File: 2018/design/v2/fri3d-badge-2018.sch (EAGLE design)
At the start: 136 parts

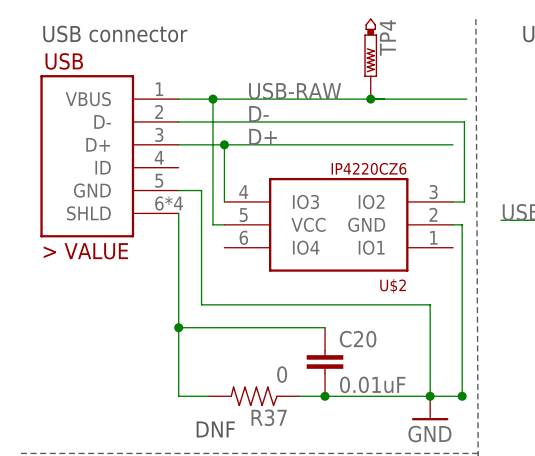
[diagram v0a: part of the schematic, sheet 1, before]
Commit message: fixed incorrect footprint for sx1308
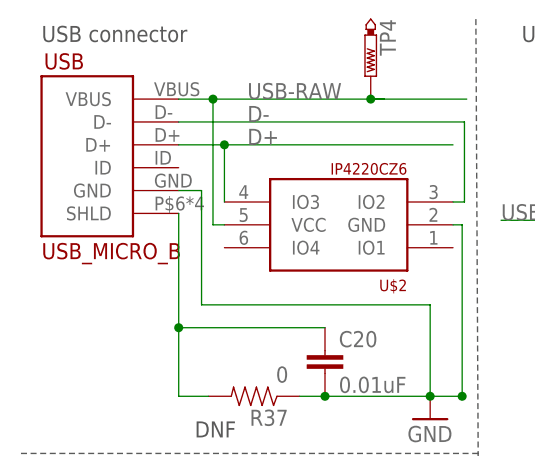
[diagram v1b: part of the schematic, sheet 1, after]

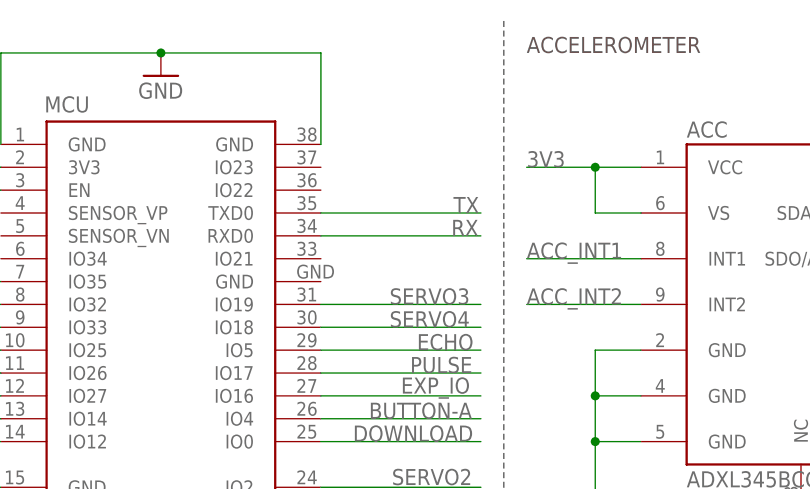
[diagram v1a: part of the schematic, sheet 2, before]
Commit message: added 3 missing traces/connections to ESP
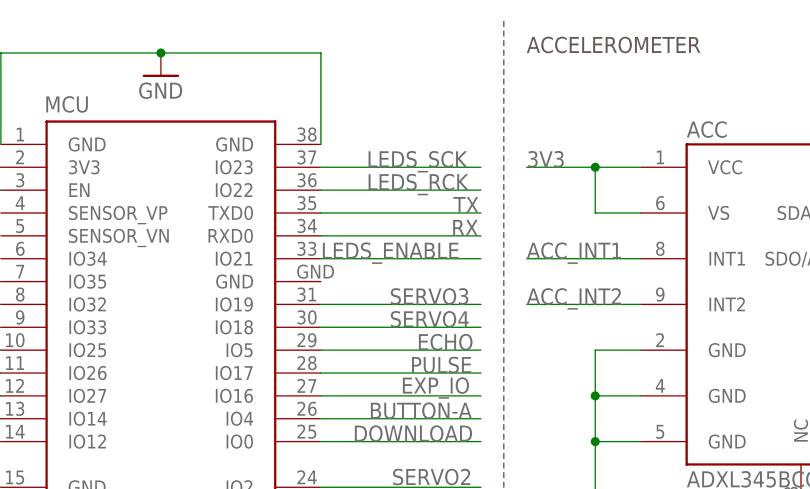
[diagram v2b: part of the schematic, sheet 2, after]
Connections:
- net LEDS_ENABLE: now also MCU.IO21
- net LEDS_RCK: now also MCU.IO22
- net LEDS_SCK: now also MCU.IO23
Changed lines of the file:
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@@
 <label x="2.54" y="7.62" size="1.778" layer="95"/>
+</segment>
+<segment>
+<pinref part="MCU" gate="G$1" pin="IO23"/>
+<wire x1="53.34" y1="162.56" x2="71.12" y2="162.56" width="0.1524" layer="91"/>
+<label x="58.42" y="162.56" size="1.778" layer="95"/>
 </segment>
 </net>
@@
 <pinref part="C19" gate="G$1" pin="2"/>
 <junction x="127" y="15.24"/>
+</segment>
+<segment>
+<pinref part="MCU" gate="G$1" pin="IO22"/>
+<wire x1="53.34" y1="160.02" x2="71.12" y2="160.02" width="0.1524" layer="91"/>
+<label x="58.42" y="160.02" size="1.778" layer="95"/>
 </segment>
 </net>
@@
 <label x="2.54" y="2.54" size="1.778" layer="95"/>
 </segment>
+<segment>
+<pinref part="MCU" gate="G$1" pin="IO21"/>
+<wire x1="53.34" y1="152.4" x2="71.12" y2="152.4" width="0.1524" layer="91"/>
+<label x="53.34" y="152.4" size="1.778" layer="95"/>
+</segment>
 </net>

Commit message: several bugfixes in schema and layout
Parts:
- removed C19: 1uF, passive:CAP0805
- removed EXP: (no value), SparkFun-Connectors:CONN_03
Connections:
- removed net 5V_ENABLE: MCU.SD1, STEP-UP.EN
- removed net EXP_IO: EXP.3, MCU.IO16
- net 5V: no longer EXP.2
- net ACC_SCK: now also MCU.IO16; no longer MCU.IO35
- net GND: no longer C19.1, EXP.1
- net LEDS_RCK: no longer C19.2
- net VCC: now also STEP-UP.EN
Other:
- note removed: "EXPANSION HEADER"
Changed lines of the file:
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@@
 <part name="SEN" library="SparkFun-Connectors" library_urn="urn:adsk.eagle:library:513" deviceset="CONN_04" device="" package3d_urn="urn:adsk.eagle:package:38085/1"/>
 <part name="GND29" library="setup" deviceset="GND" device=""/>
-<part name="EXP" library="SparkFun-Connectors" library_urn="urn:adsk.eagle:library:513" deviceset="CONN_03" device="" package3d_urn="urn:adsk.eagle:package:38063/1"/>
-<part name="GND30" library="setup" deviceset="GND" device=""/>
 <part name="LDO_MCU" library="power" deviceset="XC6210" device=""/>
 <part name="GND31" library="setup" deviceset="GND" device=""/>
@@
 <part name="C18" library="passive" deviceset="CAP" device="0805" value="1uF"/>
 <part name="GND32" library="setup" deviceset="GND" device=""/>
-<part name="C19" library="passive" deviceset="CAP" device="0805" value="1uF"/>
-<part name="GND33" library="setup" deviceset="GND" device=""/>
 <part name="U$1" library="sound" deviceset="KLJ-1230" device=""/>
 <part name="Q1" library="mosfet" deviceset="MOSFET-N" device="REFLOW"/>
@@
 <wire x1="185.42" y1="81.788" x2="185.42" y2="91.948" width="0.1524" layer="91"/>
 <junction x="185.42" y="91.948"/>
+<pinref part="STEP-UP" gate="G$1" pin="EN"/>
+<wire x1="193.04" y1="76.708" x2="185.42" y2="76.708" width="0.1524" layer="91"/>
+<wire x1="185.42" y1="76.708" x2="185.42" y2="81.788" width="0.1524" layer="91"/>
+<junction x="185.42" y="81.788"/>
 </segment>
 <segment>
@@
 <wire x1="218.44" y1="81.788" x2="218.44" y2="91.948" width="0.1524" layer="91"/>
 <junction x="218.44" y="91.948"/>
-</segment>
-</net>
-<net name="5V_ENABLE" class="0">
-<segment>
-<pinref part="STEP-UP" gate="G$1" pin="EN"/>
-<wire x1="193.04" y1="76.708" x2="177.8" y2="76.708" width="0.1524" layer="91"/>
-<label x="177.8" y="76.708" size="1.778" layer="95"/>
 </segment>
 </net>
@@
 <wire x1="101.6" y1="109.22" x2="101.6" y2="86.36" width="0.1524" layer="97" style="shortdash"/>
 <text x="104.14" y="106.68" size="1.778" layer="97">SENSOR HEADER</text>
-<text x="2.54" y="81.28" size="1.778" layer="97">EXPANSION HEADER</text>
-<wire x1="33.02" y1="86.36" x2="33.02" y2="53.34" width="0.1524" layer="97" style="shortdash"/>
 </plain>
 <instances>
@@
 <instance part="SEN" gate="G$1" x="121.412" y="95.758"/>
 <instance part="GND29" gate="1" x="129.032" y="90.678"/>
-<instance part="EXP" gate="J$1" x="12.446" y="67.31"/>
-<instance part="GND30" gate="1" x="22.86" y="62.23"/>
-<instance part="C19" gate="G$1" x="127" y="12.7" rot="R180"/>
-<instance part="GND33" gate="1" x="127" y="4.826"/>
 </instances>
 <busses>
@@
 <wire x1="2.54" y1="7.62" x2="12.7" y2="7.62" width="0.1524" layer="91"/>
 <wire x1="12.7" y1="7.62" x2="68.58" y2="7.62" width="0.1524" layer="91"/>
-<wire x1="68.58" y1="7.62" x2="116.84" y2="7.62" width="0.1524" layer="91"/>
-<wire x1="116.84" y1="7.62" x2="116.84" y2="20.32" width="0.1524" layer="91"/>
+<wire x1="68.58" y1="7.62" x2="124.46" y2="7.62" width="0.1524" layer="91"/>
+<wire x1="124.46" y1="7.62" x2="124.46" y2="20.32" width="0.1524" layer="91"/>
 <pinref part="SHIFT3" gate="G$1" pin="SCK"/>
-<wire x1="116.84" y1="20.32" x2="129.54" y2="20.32" width="0.1524" layer="91"/>
+<wire x1="124.46" y1="20.32" x2="129.54" y2="20.32" width="0.1524" layer="91"/>
 <pinref part="SHIFT1" gate="G$1" pin="SCK"/>
 <wire x1="17.78" y1="20.32" x2="12.7" y2="20.32" width="0.1524" layer="91"/>
@@
 <pinref part="SHIFT3" gate="G$1" pin="RCK"/>
 <wire x1="129.54" y1="15.24" x2="127" y2="15.24" width="0.1524" layer="91"/>
-<wire x1="127" y1="15.24" x2="119.38" y2="15.24" width="0.1524" layer="91"/>
-<wire x1="119.38" y1="15.24" x2="119.38" y2="5.08" width="0.1524" layer="91"/>
-<wire x1="119.38" y1="5.08" x2="71.12" y2="5.08" width="0.1524" layer="91"/>
+<wire x1="127" y1="15.24" x2="127" y2="5.08" width="0.1524" layer="91"/>
+<wire x1="127" y1="5.08" x2="71.12" y2="5.08" width="0.1524" layer="91"/>
 <pinref part="SHIFT1" gate="G$1" pin="RCK"/>
 <wire x1="71.12" y1="5.08" x2="15.24" y2="5.08" width="0.1524" layer="91"/>
@@
 <junction x="71.12" y="5.08"/>
 <label x="2.54" y="5.08" size="1.778" layer="95"/>
-<pinref part="C19" gate="G$1" pin="2"/>
-<junction x="127" y="15.24"/>
 </segment>
 <segment>
@@
 <pinref part="GND29" gate="1" pin="GND"/>
 <wire x1="126.492" y1="93.218" x2="129.032" y2="93.218" width="0.1524" layer="91"/>
-</segment>
-<segment>
-<pinref part="EXP" gate="J$1" pin="1"/>
-<pinref part="GND30" gate="1" pin="GND"/>
-<wire x1="20.066" y1="64.77" x2="22.86" y2="64.77" width="0.1524" layer="91"/>
-</segment>
-<segment>
-<pinref part="C19" gate="G$1" pin="1"/>
-<pinref part="GND33" gate="1" pin="GND"/>
-<wire x1="127" y1="7.366" x2="127" y2="7.62" width="0.1524" layer="91"/>
 </segment>
 </net>
@@
 </segment>
 <segment>
-<pinref part="MCU" gate="G$1" pin="IO35"/>
-<wire x1="17.78" y1="149.86" x2="2.54" y2="149.86" width="0.1524" layer="91"/>
-<label x="2.54" y="149.86" size="1.778" layer="95"/>
+<pinref part="MCU" gate="G$1" pin="IO16"/>
+<wire x1="53.34" y1="137.16" x2="71.12" y2="137.16" width="0.1524" layer="91"/>
+<label x="60.96" y="137.16" size="1.778" layer="95"/>
 </segment>
 </net>
@@
 <label x="129.032" y="100.838" size="1.778" layer="95"/>
 </segment>
-<segment>
-<pinref part="EXP" gate="J$1" pin="2"/>
-<wire x1="20.066" y1="67.31" x2="28.194" y2="67.31" width="0.1524" layer="91"/>
-<label x="20.828" y="67.31" size="1.778" layer="95"/>
-</segment>
 </net>
 <net name="SERVO2" class="0">
@@
 </segment>
 </net>
-<net name="EXP_IO" class="0">
-<segment>
-<pinref part="EXP" gate="J$1" pin="3"/>
-<wire x1="20.066" y1="69.85" x2="28.448" y2="69.85" width="0.1524" layer="91"/>
-<label x="20.828" y="69.85" size="1.778" layer="95"/>
-</segment>
-<segment>
-<pinref part="MCU" gate="G$1" pin="IO16"/>
-<wire x1="53.34" y1="137.16" x2="71.12" y2="137.16" width="0.1524" layer="91"/>
-<label x="62.23" y="137.414" size="1.778" layer="95"/>
-</segment>
-</net>
 <net name="3V3_MCU" class="0">
 <segment>
@@
 </segment>
 </net>
-<net name="5V_ENABLE" class="0">
-<segment>
-<pinref part="MCU" gate="G$1" pin="SD1"/>
-<wire x1="53.34" y1="121.92" x2="71.12" y2="121.92" width="0.1524" layer="91"/>
-<label x="57.404" y="122.174" size="1.778" layer="95"/>
-</segment>
-</net>

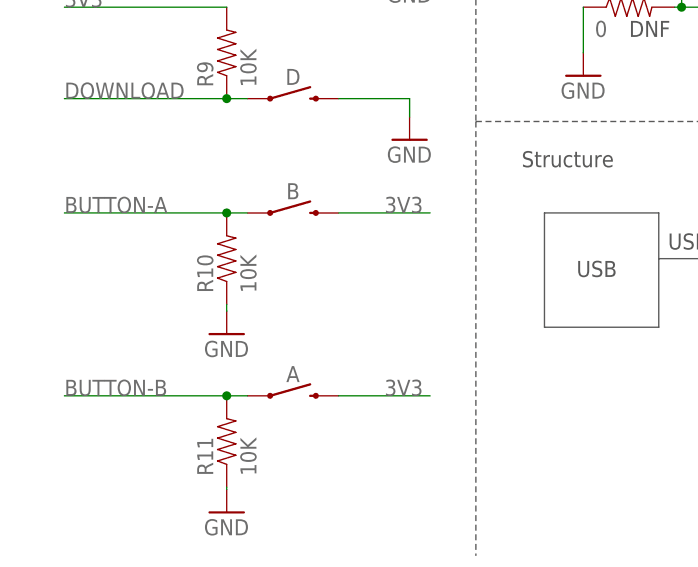
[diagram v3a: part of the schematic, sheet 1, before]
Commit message: "fixed" incorrect labels ;-)
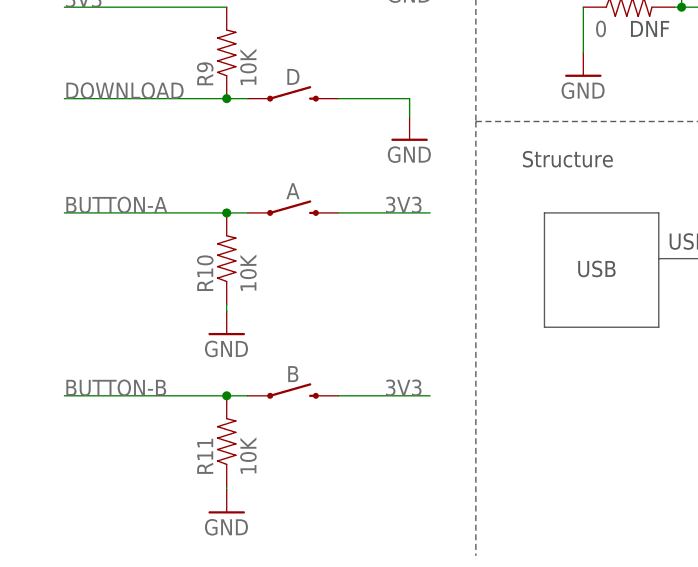
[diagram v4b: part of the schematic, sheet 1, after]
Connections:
- net BUTTON-A: now also A.1; no longer B.1
- net BUTTON-B: now also B.1; no longer A.1
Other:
- moved on the sheet: A, B
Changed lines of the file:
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@@
 <part name="R" library="switches" deviceset="SWITCH-MOMENTARY-4.5MM" device=""/>
 <part name="D" library="switches" deviceset="SWITCH-MOMENTARY-4.5MM" device=""/>
+<part name="A" library="switches" deviceset="SWITCH-MOMENTARY-4.5MM" device=""/>
 <part name="B" library="switches" deviceset="SWITCH-MOMENTARY-4.5MM" device=""/>
-<part name="A" library="switches" deviceset="SWITCH-MOMENTARY-4.5MM" device=""/>
 <part name="GND11" library="setup" deviceset="GND" device=""/>
 <part name="GND12" library="setup" deviceset="GND" device=""/>
@@
 <instance part="R" gate="G$1" x="30.48" y="68.58"/>
 <instance part="D" gate="G$1" x="30.48" y="50.8"/>
-<instance part="B" gate="G$1" x="30.48" y="38.1"/>
-<instance part="A" gate="G$1" x="30.48" y="17.78"/>
+<instance part="A" gate="G$1" x="30.48" y="38.1"/>
+<instance part="B" gate="G$1" x="30.48" y="17.78"/>
 <instance part="GND11" gate="1" x="43.434" y="64.008"/>
 <instance part="GND12" gate="1" x="43.434" y="46.228"/>
@@
 </segment>
 <segment>
-<pinref part="B" gate="G$1" pin="2"/>
+<pinref part="A" gate="G$1" pin="2"/>
 <wire x1="35.56" y1="38.1" x2="45.72" y2="38.1" width="0.1524" layer="91"/>
 <label x="40.64" y="38.1" size="1.778" layer="95"/>
 </segment>
 <segment>
-<pinref part="A" gate="G$1" pin="2"/>
+<pinref part="B" gate="G$1" pin="2"/>
 <wire x1="35.56" y1="17.78" x2="45.72" y2="17.78" width="0.1524" layer="91"/>
 <label x="40.64" y="17.78" size="1.778" layer="95"/>
@@
 <net name="BUTTON-A" class="0">
 <segment>
-<pinref part="B" gate="G$1" pin="1"/>
+<pinref part="A" gate="G$1" pin="1"/>
 <wire x1="25.4" y1="38.1" x2="23.114" y2="38.1" width="0.1524" layer="91"/>
 <label x="5.08" y="38.1" size="1.778" layer="95"/>
@@
 <net name="BUTTON-B" class="0">
 <segment>
-<pinref part="A" gate="G$1" pin="1"/>
+<pinref part="B" gate="G$1" pin="1"/>
 <wire x1="25.4" y1="17.78" x2="23.114" y2="17.78" width="0.1524" layer="91"/>
 <label x="5.08" y="17.78" size="1.778" layer="95"/>
